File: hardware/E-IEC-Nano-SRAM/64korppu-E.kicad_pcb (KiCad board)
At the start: 2 copper layers, 140 x 120 mm, 27 parts, among them J1 DIN-6_IEC, J2 Floppy_34pin, J3 DC_Jack, U1 Arduino_Nano, U2 23LC1024, U3 74HC595

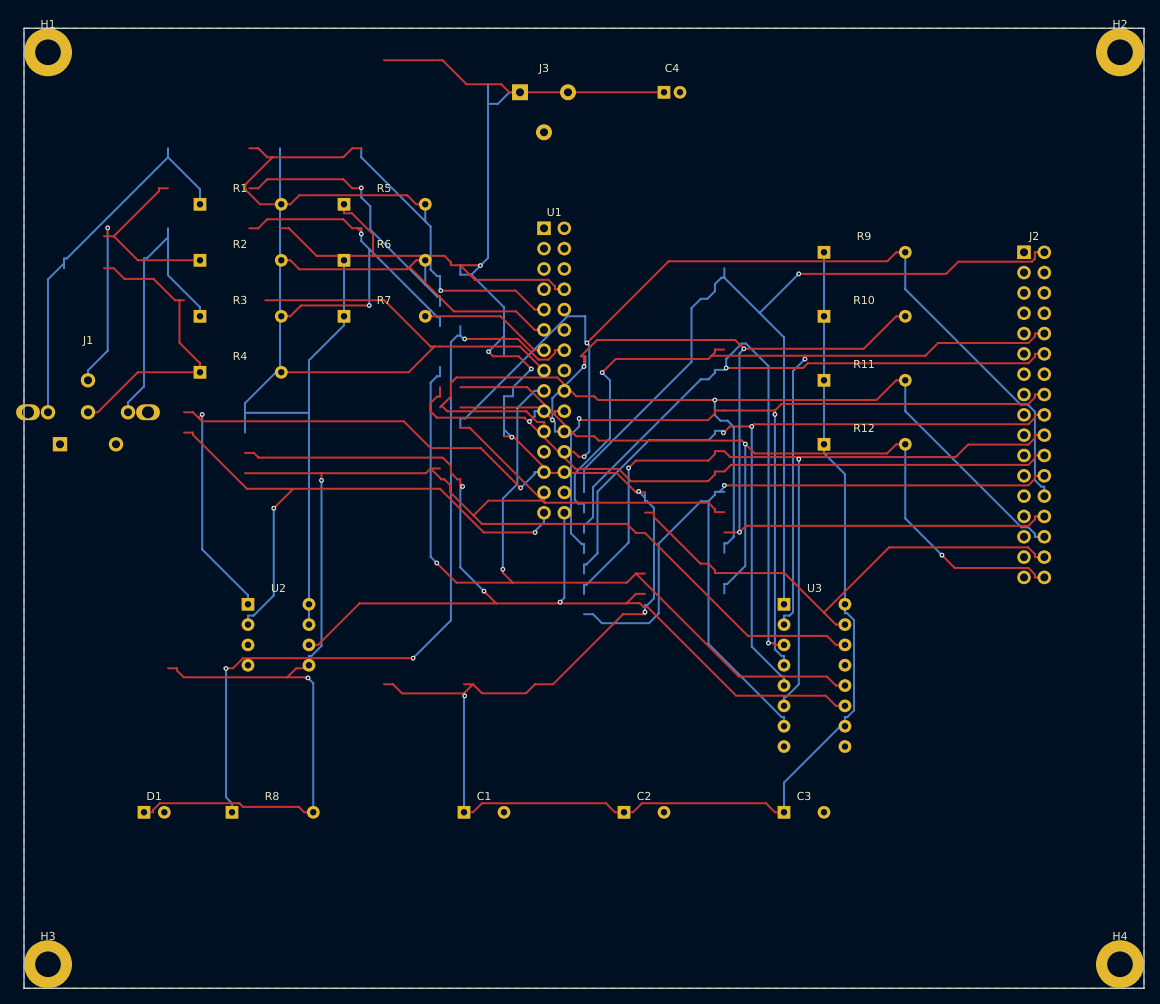
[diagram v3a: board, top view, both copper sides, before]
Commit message: Convert PCB to 4-layer 70x60mm (75% smaller)
- 4 layers: F.Cu/In1.Cu(GND)/In2.Cu(+5V)/B.Cu
- Board size reduced from 140x120mm to 70x60mm
- Dedicated GND and VCC power planes on inner layers
- All signals routed, 2 minor +5V zone connectivity issues
- Add convert-4layer.py script for 2→4 layer conversion
- Update pipeline for 4-layer Gerber export (In1.Cu, In2.Cu)

Co-Authored-By: Claude Opus 4.6 <noreply@anthropic.com>
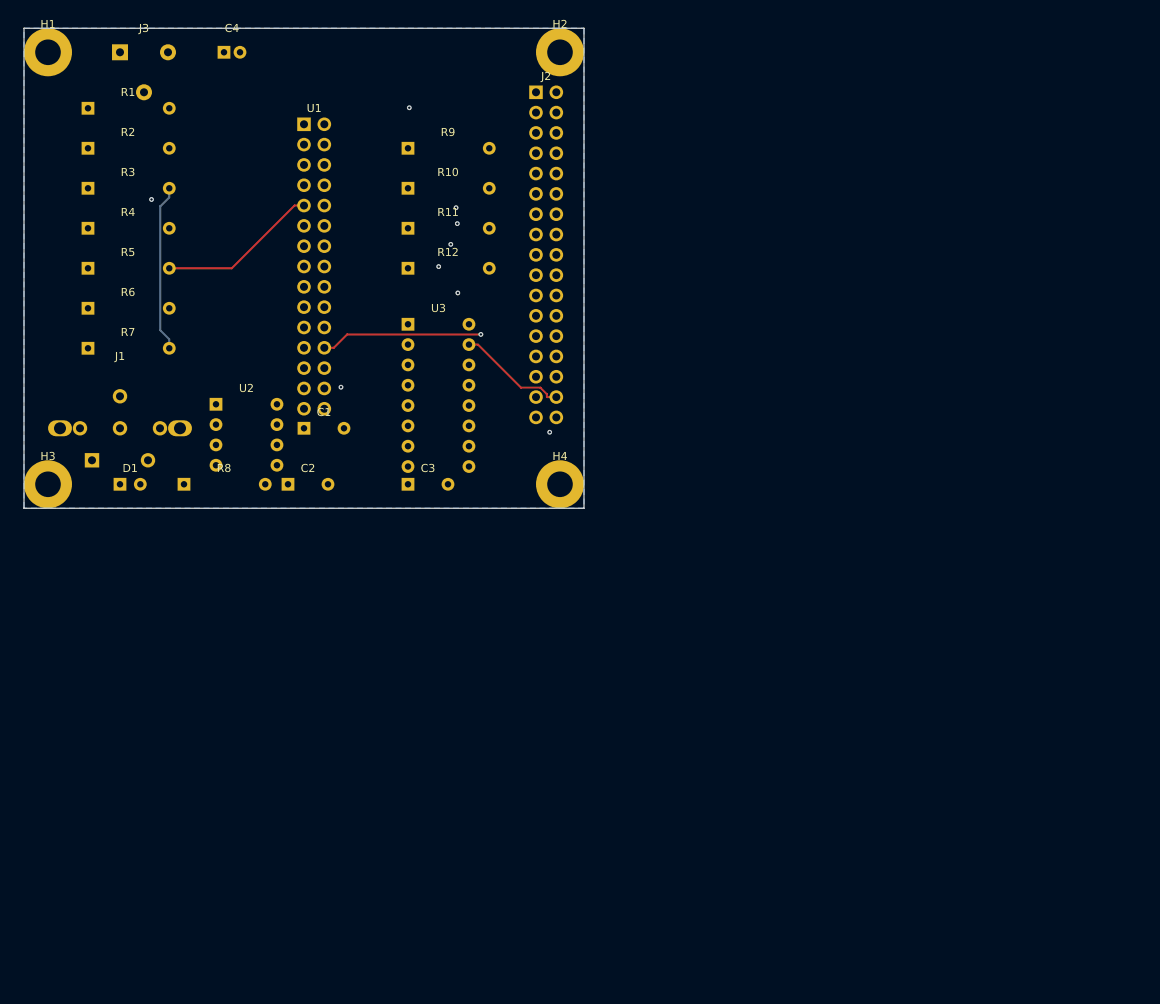
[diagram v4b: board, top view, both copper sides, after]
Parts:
- moved H4 92.2 mm to (167.0, 157.0)
- moved H2 70.0 mm to (167.0, 103.0)
- moved J2 64.2 mm to (164.0, 108.0)
- moved C3 62.4 mm to (148.0, 157.0)
- moved H3 60.0 mm to (103.0, 157.0)
- moved C2 58.7 mm to (133.0, 157.0)
- moved U3 58.6 mm to (148.0, 137.0)
- moved R12 56.5 mm to (148.0, 130.0)
- moved R11 55.4 mm to (148.0, 125.0)
- moved C4 55.2 mm to (125.0, 103.0)
- moved R10 54.4 mm to (148.0, 120.0)
- moved R9 53.6 mm to (148.0, 115.0)
- moved C1 52.0 mm to (135.0, 150.0)
- moved J3 50.2 mm to (112.0, 103.0)
- moved R8 41.4 mm to (120.0, 157.0)
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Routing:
- net +5V: track 457.0 -> 0.00 mm, vias 7 -> 0
- net SPI_MOSI: track 159.2 -> 33.4 mm, vias 1 -> 0
- net SPI_SCK: track 135.9 -> 27.6 mm, vias 3 -> 0
- net FLOPPY_MOTEA: track 115.3 -> 34.5 mm, vias 2 -> 1
- net FLOPPY_DRVSEL: track 115.1 -> 34.5 mm, vias 2 -> 1
- net LATCH_595: track 112.3 -> 32.2 mm, vias 2 -> 1
- net FLOPPY_MOTOR: track 110.6 -> 34.9 mm, vias 2 -> 1
- net FLOPPY_WPT: track 134.2 -> 60.0 mm, vias 4 -> 0
- net FLOPPY_STEP: track 105.0 -> 32.8 mm, vias 2 -> 1
- net FLOPPY_TRK00: track 125.7 -> 54.6 mm, vias 2 -> 1
- net FLOPPY_DIR: track 106.2 -> 35.7 mm, vias 2 -> 1
- net FLOPPY_DENSITY: track 119.1 -> 48.7 mm
- net FLOPPY_WGATE: track 104.1 -> 36.1 mm
- net FLOPPY_RDATA: track 127.0 -> 59.4 mm, vias 1 -> 0
- net SPI_CS_SRAM: track 76.6 -> 12.9 mm, vias 2 -> 0
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- added copper zone on In2.Cu, net +5V
- added copper zone on In1.Cu, net GND
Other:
- board size 140 x 120 mm -> 70 x 60 mm
- copper layers 2 -> 4
